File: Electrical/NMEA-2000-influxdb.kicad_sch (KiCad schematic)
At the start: 8 parts, among them U1 LM7805_TO220, U2 SN65HVD230-Module, U3 RTC-Module, U4 BMP280-Module, U5 SD-Card-Module

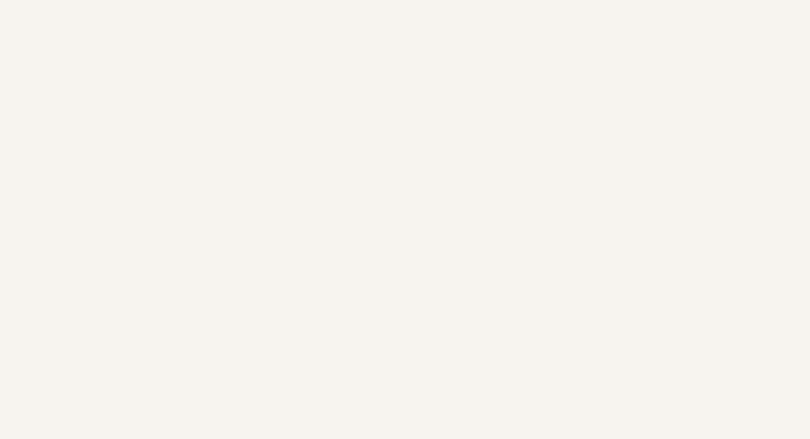
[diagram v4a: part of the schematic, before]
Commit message: Added Power Connector
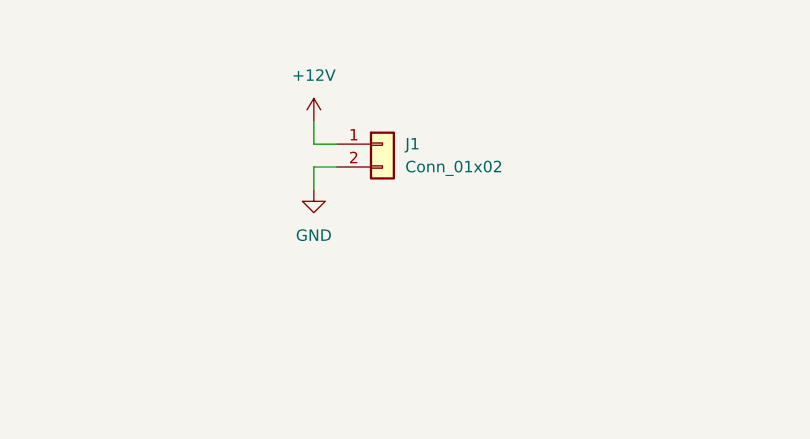
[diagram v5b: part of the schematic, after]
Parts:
- added J1: Conn_01x02, Capacitor_THT:CP_Radial_D8.0mm_P5.00mm, symbol Connector_Generic:Conn_01x02
- C1, C2: footprint (none) -> Capacitor_THT:CP_Radial_D8.0mm_P5.00mm
- U2: footprint (none) -> Connector_PinSocket_2.54mm:PinSocket_1x04_P2.54mm_Vertical
- U3, U4, U5: footprint (none) -> Connector_PinSocket_2.54mm:PinSocket_1x06_P2.54mm_Vertical
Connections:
- net +12V: now also J1.1 (Pin_1)
- net GND: now also J1.2 (Pin_2)
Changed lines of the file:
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@@
+    (stroke (width 0) (type default))
+  )
+  (wire (pts (xy 69.85 45.72) (xy 67.31 45.72))
     (stroke (width 0) (type default))
   )
@@
     (stroke (width 0) (type default))
   )
+  (wire (pts (xy 69.85 48.26) (xy 67.31 48.26))
+    (stroke (width 0) (type default))
+  )
   (wire (pts (xy 227.33 68.58) (xy 224.79 68.58))
     (stroke (width 0) (type default))
@@
     (stroke (width 0) (type default))
   )
+  (wire (pts (xy 67.31 43.18) (xy 67.31 45.72))
+    (stroke (width 0) (type default))
+  )
   (wire (pts (xy 219.71 71.12) (xy 227.33 71.12))
     (stroke (width 0) (type default))
@@
   )
   (wire (pts (xy 213.36 139.7) (xy 220.98 139.7))
+    (stroke (width 0) (type default))
+  )
+  (wire (pts (xy 67.31 48.26) (xy 67.31 50.8))
     (stroke (width 0) (type default))
   )
@@
       (effects (font (size 1.27 1.27)) (justify left))
     )
-    (property "Footprint" "" (at 216.154 45.466 0)
+    (property "Footprint" "Capacitor_THT:CP_Radial_D8.0mm_P5.00mm" (at 216.154 45.466 0)
       (effects (font (size 1.27 1.27)) hide)
     )
@@
     )
   )
+  (symbol (lib_id "power:+12V") (at 67.31 43.18 0) (unit 1)
+    (in_bom yes) (on_board yes) (dnp no) (fields_autoplaced)
+    (property "Reference" "#PWR015" (at 67.31 46.99 0)
+      (effects (font (size 1.27 1.27)) hide)
+    )
+    (property "Value" "+12V" (at 67.31 38.1 0)
+      (effects (font (size 1.27 1.27)))
+    )
+    (property "Footprint" "" (at 67.31 43.18 0)
+      (effects (font (size 1.27 1.27)) hide)
+    )
+    (property "Datasheet" "" (at 67.31 43.18 0)
+      (effects (font (size 1.27 1.27)) hide)
+    )
+    (pin "1")
+    (instances
+      (project "NMEA-2000-influxdb"
+        (path "/efe7a42c-525a-4afc-8476-4cc785240ca6"
+          (reference "#PWR015") (unit 1)
+        )
+      )
+    )
+  )
   (symbol (lib_id "power:GND") (at 210.82 144.78 0) (unit 1)
     (in_bom yes) (on_board yes) (dnp no) (fields_autoplaced)
@@
       (effects (font (size 1.27 1.27)) (justify left))
     )
-    (property "Footprint" "" (at 234.95 96.52 0)
+    (property "Footprint" "Connector_PinSocket_2.54mm:PinSocket_1x06_P2.54mm_Vertical" (at 234.95 96.52 0)
       (effects (font (size 1.27 1.27)) hide)
     )
@@
       (effects (font (size 1.27 1.27)) (justify left))
     )
-    (property "Footprint" "" (at 234.95 62.23 0)
+    (property "Footprint" "Connector_PinSocket_2.54mm:PinSocket_1x06_P2.54mm_Vertical" (at 234.95 62.23 0)
       (effects (font (size 1.27 1.27)) hide)
     )
@@
       (effects (font (size 1.27 1.27)) (justify left))
     )
-    (property "Footprint" "" (at 236.474 45.466 0)
+    (property "Footprint" "Capacitor_THT:CP_Radial_D8.0mm_P5.00mm" (at 236.474 45.466 0)
       (effects (font (size 1.27 1.27)) hide)
     )
@@
     )
   )
+  (symbol (lib_id "Connector_Generic:Conn_01x02") (at 74.93 45.72 0) (unit 1)
+    (in_bom yes) (on_board yes) (dnp no) (fields_autoplaced)
+    (property "Reference" "J1" (at 77.47 45.72 0)
+      (effects (font (size 1.27 1.27)) (justify left))
+    )
+    (property "Value" "Conn_01x02" (at 77.47 48.26 0)
+      (effects (font (size 1.27 1.27)) (justify left))
+    )
+    (property "Footprint" "Capacitor_THT:CP_Radial_D8.0mm_P5.00mm" (at 74.93 45.72 0)
+      (effects (font (size 1.27 1.27)) hide)
+    )
+    (property "Datasheet" "~" (at 74.93 45.72 0)
+      (effects (font (size 1.27 1.27)) hide)
+    )
+    (pin "1")
+    (pin "2")
+    (instances
+      (project "NMEA-2000-influxdb"
+        (path "/efe7a42c-525a-4afc-8476-4cc785240ca6"
+          (reference "J1") (unit 1)
+        )
+      )
+    )
+  )
   (symbol (lib_id "power:GND") (at 226.314 53.086 0) (unit 1)
     (in_bom yes) (on_board yes) (dnp no) (fields_autoplaced)
@@
       (effects (font (size 1.27 1.27)))
     )
-    (property "Footprint" "" (at 231.14 132.08 0)
+    (property "Footprint" "Connector_PinSocket_2.54mm:PinSocket_1x04_P2.54mm_Vertical" (at 231.14 132.08 0)
       (effects (font (size 1.27 1.27)) hide)
     )
@@
       (effects (font (size 1.27 1.27)))
     )
-    (property "Footprint" "" (at 35.56 93.98 0)
+    (property "Footprint" "Connector_PinSocket_2.54mm:PinSocket_1x06_P2.54mm_Vertical" (at 35.56 93.98 0)
       (effects (font (size 1.27 1.27)) hide)
     )
@@
         )
       )
+    )
+  )
+  (symbol (lib_id "power:GND") (at 67.31 50.8 0) (unit 1)
+    (in_bom yes) (on_board yes) (dnp no) (fields_autoplaced)
+    (property "Reference" "#PWR016" (at 67.31 57.15 0)
+      (effects (font (size 1.27 1.27)) hide)
+    )
+    (property "Value" "GND" (at 67.31 55.88 0)
+      (effects (font (size 1.27 1.27)))
+    )
+    (property "Footprint" "" (at 67.31 50.8 0)
+      (effects (font (size 1.27 1.27)) hide)
+    )
+    (property "Datasheet" "" (at 67.31 50.8 0)
+      (effects (font (size 1.27 1.27)) hide)
+    )
+    (pin "1")
+    (instances
+      (project "NMEA-2000-influxdb"
+        (path "/efe7a42c-525a-4afc-8476-4cc785240ca6"
+          (reference "#PWR016") (unit 1)
+        )
+      )

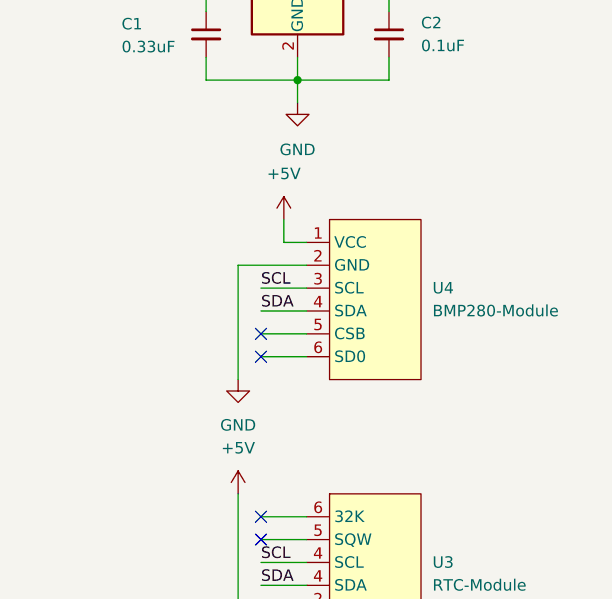
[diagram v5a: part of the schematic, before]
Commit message: Removed BMP280 Sensor
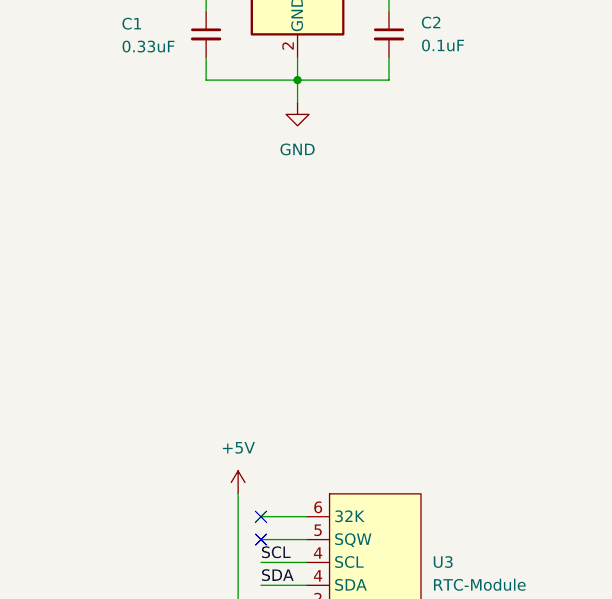
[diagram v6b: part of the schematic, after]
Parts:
- removed U4: BMP280-Module, Connector_PinSocket_2.54mm:PinSocket_1x06_P2.54mm_Vertical, symbol BMP280-Module:BMP280-Module
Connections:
- no-connect marks 4 -> 2
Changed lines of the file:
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@@
   )
   (no_connect (at 222.25 99.06))
-  (no_connect (at 222.25 81.28))
   (no_connect (at 222.25 101.6))
-  (no_connect (at 222.25 78.74))
   (wire (pts (xy 125.73 111.76) (xy 120.65 111.76))
     (stroke (width 0) (type default))
@@
     (stroke (width 0) (type default))
   )
-  (wire (pts (xy 222.25 81.28) (xy 227.33 81.28))
-    (stroke (width 0) (type default))
-  )
-  (wire (pts (xy 222.25 76.2) (xy 227.33 76.2))
-    (stroke (width 0) (type default))
-  )
   (wire (pts (xy 151.13 111.76) (xy 156.21 111.76))
     (stroke (width 0) (type default))
@@
     (stroke (width 0) (type default))
   )
-  (wire (pts (xy 227.33 68.58) (xy 224.79 68.58))
-    (stroke (width 0) (type default))
-  )
   (wire (pts (xy 236.474 50.546) (xy 236.474 48.006))
     (stroke (width 0) (type default))
@@
     (stroke (width 0) (type default))
   )
-  (wire (pts (xy 219.71 71.12) (xy 227.33 71.12))
-    (stroke (width 0) (type default))
-  )
   (wire (pts (xy 43.18 114.3) (xy 50.8 114.3))
     (stroke (width 0) (type default))
@@
     (stroke (width 0) (type default))
   )
-  (wire (pts (xy 222.25 78.74) (xy 227.33 78.74))
-    (stroke (width 0) (type default))
-  )
   (wire (pts (xy 125.73 114.3) (xy 120.65 114.3))
     (stroke (width 0) (type default))
@@
     (stroke (width 0) (type default))
   )
-  (wire (pts (xy 222.25 73.66) (xy 227.33 73.66))
-    (stroke (width 0) (type default))
-  )
   (wire (pts (xy 50.8 111.76) (xy 43.18 111.76))
     (stroke (width 0) (type default))
@@
     (stroke (width 0) (type default))
   )
-  (wire (pts (xy 219.71 83.82) (xy 219.71 71.12))
-    (stroke (width 0) (type default))
-  )
   (wire (pts (xy 120.65 129.54) (xy 125.73 129.54))
     (stroke (width 0) (type default))
@@
     (stroke (width 0) (type default))
   )
-  (wire (pts (xy 224.79 68.58) (xy 224.79 66.04))
-    (stroke (width 0) (type default))
-  )
   (wire (pts (xy 158.75 114.3) (xy 151.13 114.3))
     (stroke (width 0) (type default))
@@
   )
   (label "SCL" (at 120.65 129.54 0) (fields_autoplaced)
-    (effects (font (size 1.27 1.27)) (justify left bottom))
-  )
-  (label "SDA" (at 222.25 76.2 0) (fields_autoplaced)
     (effects (font (size 1.27 1.27)) (justify left bottom))
   )
@@
   )
   (label "CAN_TX" (at 118.11 121.92 0) (fields_autoplaced)
-    (effects (font (size 1.27 1.27)) (justify left bottom))
-  )
-  (label "SCL" (at 222.25 73.66 0) (fields_autoplaced)
     (effects (font (size 1.27 1.27)) (justify left bottom))
   )
@@
         (path "/efe7a42c-525a-4afc-8476-4cc785240ca6"
           (reference "U3") (unit 1)
-        )
-      )
-    )
-  )
-  (symbol (lib_id "BMP280-Module:BMP280-Module") (at 234.95 62.23 0) (unit 1)
-    (in_bom yes) (on_board yes) (dnp no) (fields_autoplaced)
-    (property "Reference" "U4" (at 241.3 73.66 0)
-      (effects (font (size 1.27 1.27)) (justify left))
-    )
-    (property "Value" "BMP280-Module" (at 241.3 76.2 0)
-      (effects (font (size 1.27 1.27)) (justify left))
-    )
-    (property "Footprint" "Connector_PinSocket_2.54mm:PinSocket_1x06_P2.54mm_Vertical" (at 234.95 62.23 0)
-      (effects (font (size 1.27 1.27)) hide)
-    )
-    (property "Datasheet" "" (at 234.95 62.23 0)
-      (effects (font (size 1.27 1.27)) hide)
-    )
-    (pin "1")
-    (pin "2")
-    (pin "3")
-    (pin "4")
-    (pin "5")
-    (pin "6")
-    (instances
-      (project "NMEA-2000-influxdb"
-        (path "/efe7a42c-525a-4afc-8476-4cc785240ca6"
-          (reference "U4") (unit 1)
         )
       )
@@
     )
   )
-  (symbol (lib_id "power:+5V") (at 224.79 66.04 0) (unit 1)
-    (in_bom yes) (on_board yes) (dnp no) (fields_autoplaced)
-    (property "Reference" "#PWR011" (at 224.79 69.85 0)
-      (effects (font (size 1.27 1.27)) hide)
-    )
-    (property "Value" "+5V" (at 224.79 60.96 0)
-      (effects (font (size 1.27 1.27)))
-    )
-    (property "Footprint" "" (at 224.79 66.04 0)
-      (effects (font (size 1.27 1.27)) hide)
-    )
-    (property "Datasheet" "" (at 224.79 66.04 0)
-      (effects (font (size 1.27 1.27)) hide)
-    )
-    (pin "1")
-    (instances
-      (project "NMEA-2000-influxdb"
-        (path "/efe7a42c-525a-4afc-8476-4cc785240ca6"
-          (reference "#PWR011") (unit 1)
-        )
-      )
-    )
-  )
   (symbol (lib_id "power:+5V") (at 50.8 99.06 0) (unit 1)
     (in_bom yes) (on_board yes) (dnp no) (fields_autoplaced)
@@
         )
       )
-    )
-  )
-  (symbol (lib_id "power:GND") (at 219.71 83.82 0) (unit 1)
-    (in_bom yes) (on_board yes) (dnp no) (fields_autoplaced)
-    (property "Reference" "#PWR012" (at 219.71 90.17 0)
-      (effects (font (size 1.27 1.27)) hide)
-    )
-    (property "Value" "GND" (at 219.71 88.9 0)
-      (effects (font (size 1.27 1.27)))
-    )
-    (property "Footprint" "" (at 219.71 83.82 0)
-      (effects (font (size 1.27 1.27)) hide)
-    )
-    (property "Datasheet" "" (at 219.71 83.82 0)
-      (effects (font (size 1.27 1.27)) hide)
-    )
-    (pin "1")
-    (instances
-      (project "NMEA-2000-influxdb"
-        (path "/efe7a42c-525a-4afc-8476-4cc785240ca6"
-          (reference "#PWR012") (unit 1)
-        )
-      )

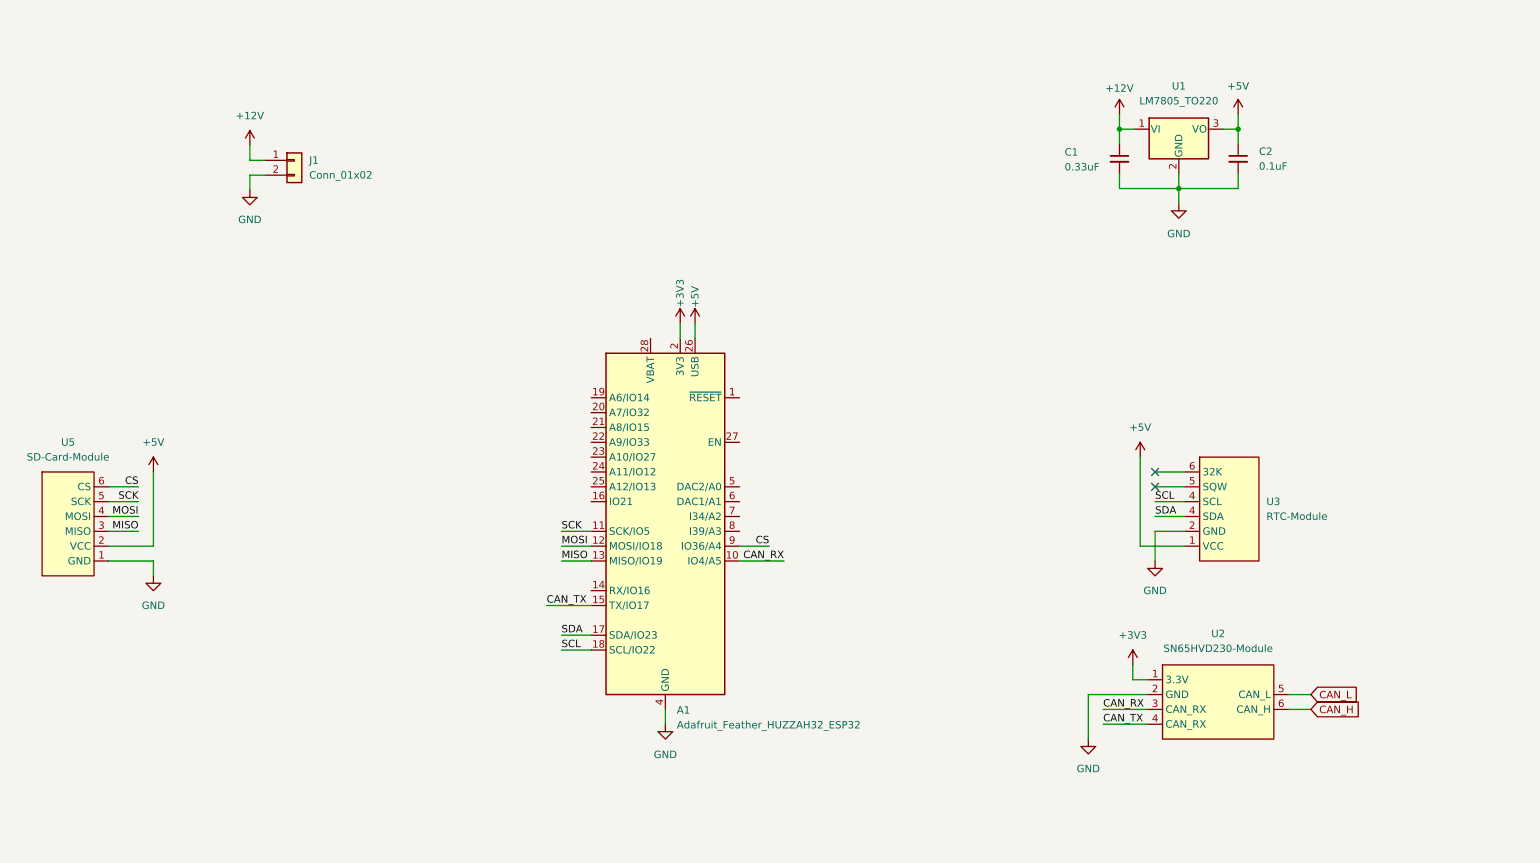
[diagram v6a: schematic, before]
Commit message: Replaced SN65HVD230-Module with SN65HVD230
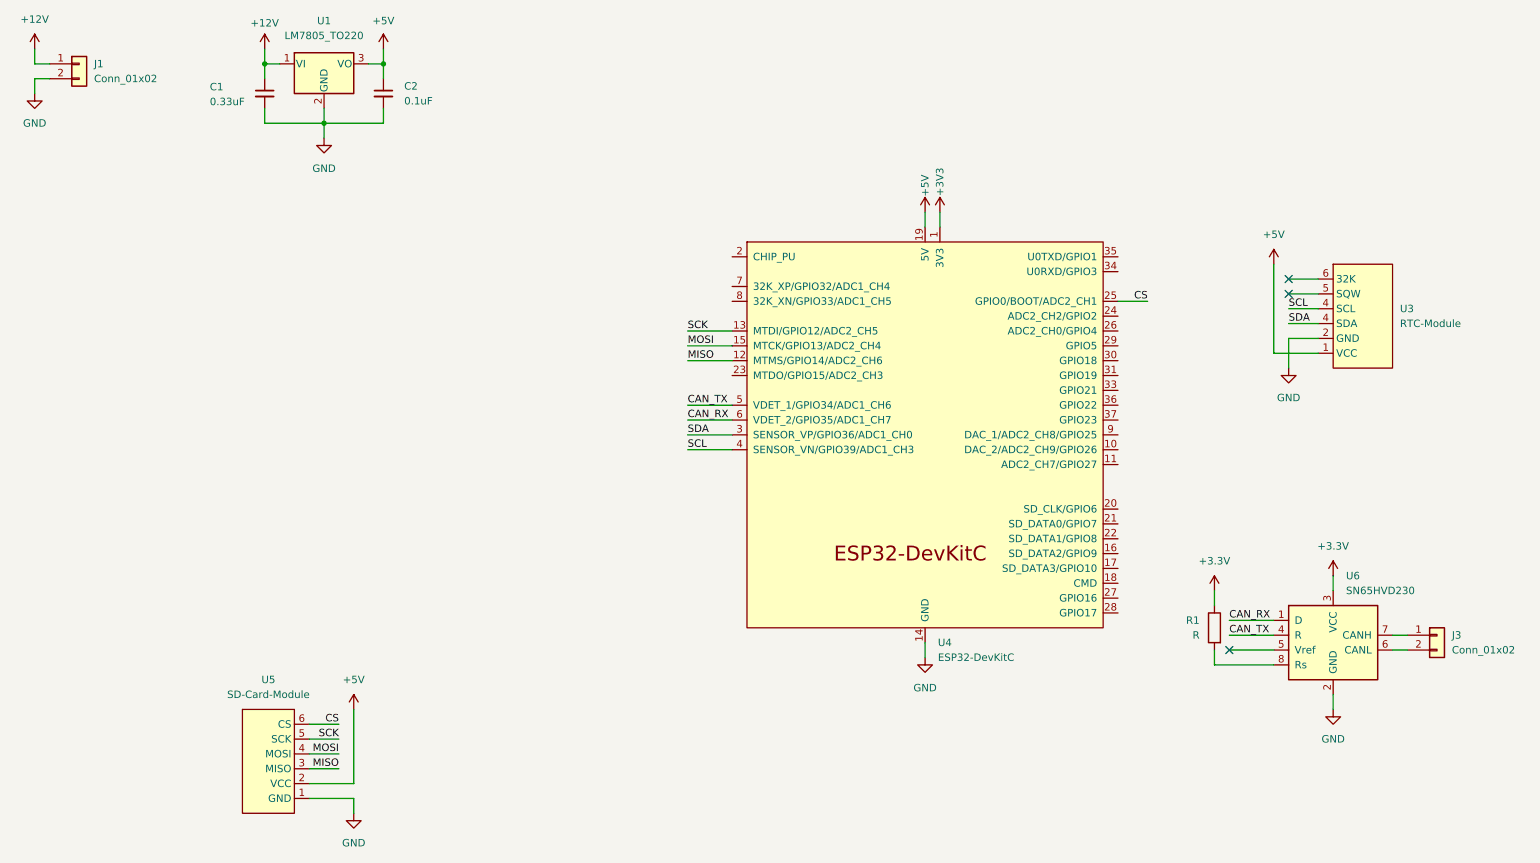
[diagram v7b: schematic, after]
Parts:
- removed A1: Adafruit_Feather_HUZZAH32_ESP32, Module:Adafruit_Feather, symbol MCU_Module:Adafruit_Feather_HUZZAH32_ESP32
- removed U2: SN65HVD230-Module, Connector_PinSocket_2.54mm:PinSocket_1x04_P2.54mm_Vertical, symbol sn65hvd230-module:SN65HVD230-Module
- added J3: Conn_01x02, symbol Connector_Generic:Conn_01x02
- added R1: R, symbol Device:R
- added U4: ESP32-DevKitC, Espressif:MODULE_ESP32_NODEMCU, symbol Espressif:ESP32-DevKitC
- added U6: SN65HVD230, Package_SO:SOIC-8_3.9x4.9mm_P1.27mm, symbol Interface_CAN_LIN:SN65HVD230
- C1, C2: footprint Capacitor_THT:CP_Radial_D8.0mm_P5.00mm -> Capacitor_THT:C_Disc_D9.0mm_W5.0mm_P7.50mm
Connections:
- net +3V3: now also U4.1 (3V3)
- net +5V: now also U4.19 (5V)
- net CAN_RX: now also U4.6 (VDET_2/GPIO35/ADC1_CH7), U6.1 (D)
- net CAN_TX: now also U4.5 (VDET_1/GPIO34/ADC1_CH6), U6.4 (R)
- net CS: now also U4.25 (GPIO0/BOOT/ADC2_CH1)
- net GND: now also U4.14 (GND), U4.32 (GND), U4.38 (GND), U6.2 (GND)
- net MISO: now also U4.12 (MTMS/GPIO14/ADC2_CH6)
- net MOSI: now also U4.15 (MTCK/GPIO13/ADC2_CH4)
- net SCK: now also U4.13 (MTDI/GPIO12/ADC2_CH5)
- net SCL: now also U4.4 (SENSOR_VN/GPIO39/ADC1_CH3)
- net SDA: now also U4.3 (SENSOR_VP/GPIO36/ADC1_CH0)
- new net: J3.2 (Pin_2), U6.6 (CANL)
- new net: J3.1 (Pin_1), U6.7 (CANH)
- new net: R1.2, U6.8 (Rs)
- new net +3.3V: R1.1, U6.3 (VCC)
- no-connect marks 2 -> 3
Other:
- moved on the sheet: C1, C2, J1, U1, U3, U5
